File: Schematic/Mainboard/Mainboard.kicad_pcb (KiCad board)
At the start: 2 copper layers, 14 parts, among them J1 Motor_C, J2 Motor_B, J3 Motor_A, J4 Servo, J5 Servo, J6 ESC, J7 ESC_PWR, SW1 SW_DIP_x01, U1 BP, U4 XL60019_Boost_Module, U5 Mini360, U6 RFM69HW

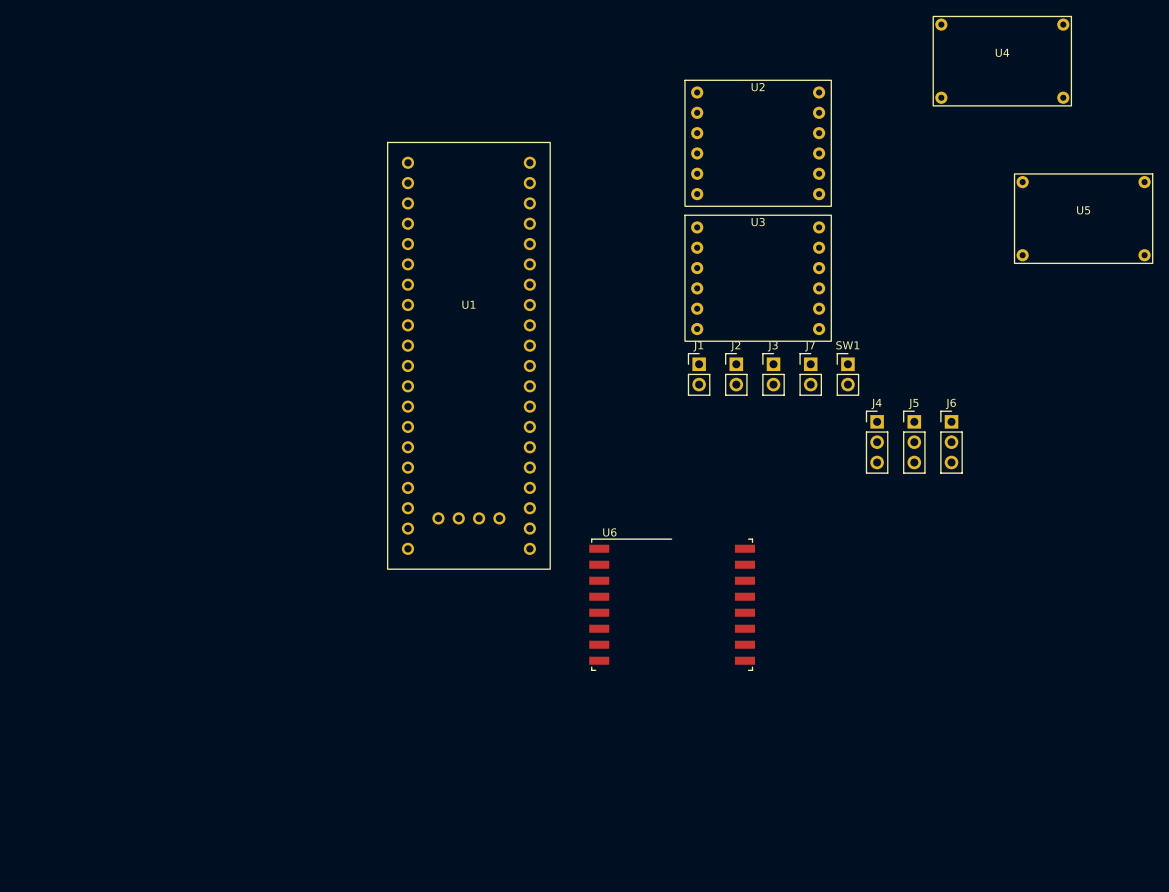
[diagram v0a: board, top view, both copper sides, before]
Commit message: PCB work
trying to cram everything on there
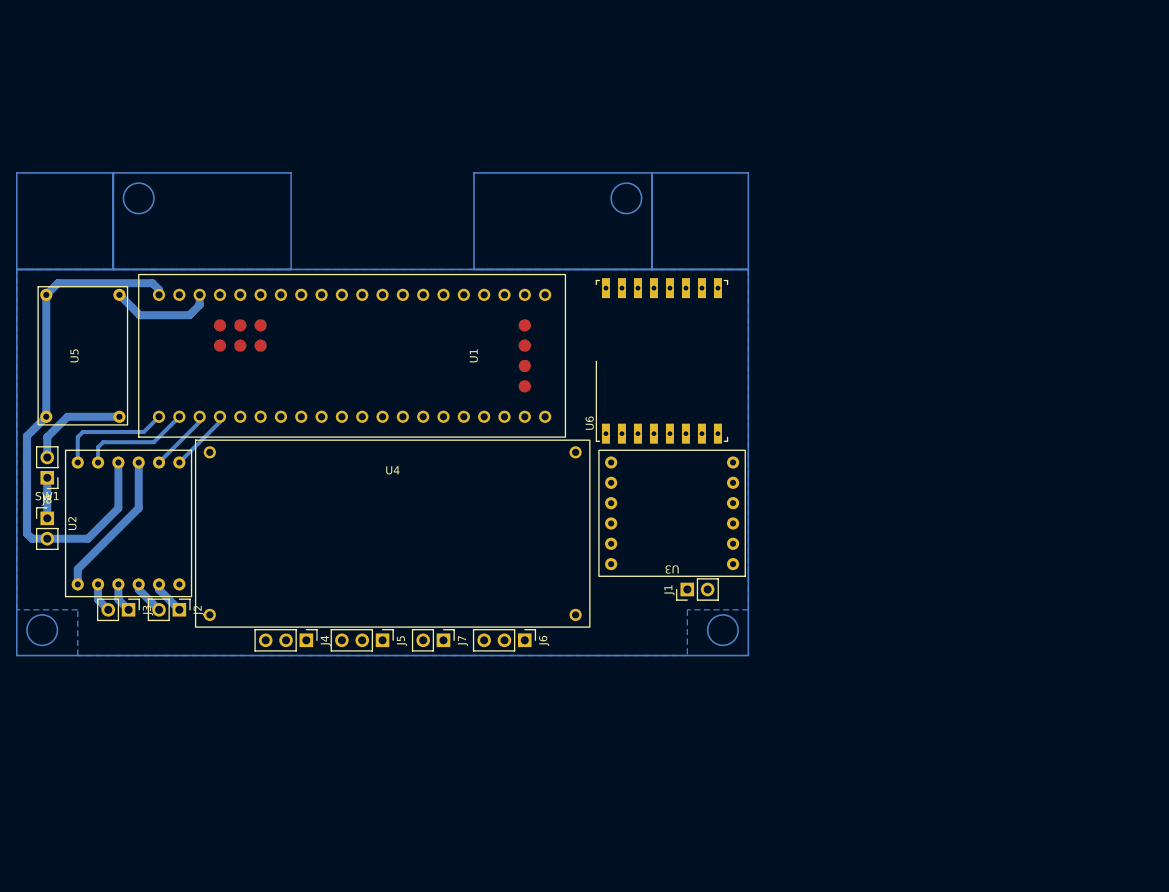
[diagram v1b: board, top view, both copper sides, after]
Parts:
- added J8: BATT_IN, Connector_PinHeader_2.54mm:PinHeader_1x02_P2.54mm_Vertical, F.Cu at (72.4, 102.9)
- SW1: value SW_DIP_x01 -> MAIN_CUTOFF
- U4: footprint My_Library:Mini360 -> My_Library:XL60019 Boost Module
- U6: footprint RF_Module:HOPERF_RFM69HW -> My_Library:HOPERF_RFM69HW
- moved U5 126.3 mm to (76.8, 82.5), turned to 90 degrees
- moved SW1 101.1 mm to (72.4, 97.8), turned to 180 degrees
- moved U4 96.2 mm to (115.6, 104.5)
- moved U2 93.7 mm to (81.3, 103.5), turned to 90 degrees
- moved J3 86.3 mm to (82.6, 114.3), turned to -90 degrees
- moved J4 76.4 mm to (104.8, 118.1), turned to -90 degrees
- moved J2 76.1 mm to (88.9, 114.3), turned to -90 degrees
- moved J5 71.9 mm to (114.3, 118.1), turned to -90 degrees
- moved J6 59.9 mm to (132.1, 118.1), turned to -90 degrees
- moved J7 57.4 mm to (121.9, 118.1), turned to -90 degrees
- moved U3 33.7 mm to (150.5, 103.5), turned to 180 degrees
- moved U6 30.5 mm to (149.2, 83.2), turned to 90 degrees
- moved J1 28.2 mm to (152.4, 111.8), turned to 90 degrees
- moved U1 15.9 mm to (109.2, 82.5), turned to 90 degrees
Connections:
- U1 pad PA0: /M B1 -> unconnected-(U1-PadPA0)
- U1 pad PA1: /M B2 -> unconnected-(U1-PadPA1)
- U1 pad PA10: unconnected-(U1-PadPA10) -> /ESC
- U1 pad PA2: /M C1 -> unconnected-(U1-PadPA2)
- U1 pad PA3: /M C2 -> unconnected-(U1-PadPA3)
- U1 pad PA8: unconnected-(U1-PadPA8) -> /SERVO 2
- U1 pad PA9: unconnected-(U1-PadPA9) -> /SERVO 1
- U1 pad PB12: unconnected-(U1-PadPB12) -> /M B2
- U1 pad PB13: unconnected-(U1-PadPB13) -> /M B1
- U1 pad PB14: unconnected-(U1-PadPB14) -> /M A2
- U1 pad PB15: unconnected-(U1-PadPB15) -> /M A1
- U1 pad PB7: /ESC -> unconnected-(U1-PadPB7)
- U1 pad PB8: /SERVO 2 -> /M C2
- U1 pad PB9: /SERVO 1 -> /M C1
- U1 pad PC14: /M A1 -> unconnected-(U1-PadPC14)
- U1 pad PC15: /M A2 -> unconnected-(U1-PadPC15)
- U1 pad SWO: (no net) -> unconnected-(U1-PadSWO)
- U2 pad 1: +3V3 -> +12V
- U3 pad 1: +3V3 -> +12V
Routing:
- net GND: track 0.00 -> 65.5 mm
- net +12V: track 0.00 -> 18.4 mm
- net /M B2: track 0.00 -> 14.4 mm
- net /M B1: track 0.00 -> 13.6 mm
- net +3V3: track 0.00 -> 12.9 mm
- net /+BATT SW: track 0.00 -> 12.6 mm
- net /M A2: track 0.00 -> 7.82 mm
- net /M A1: track 0.00 -> 7.82 mm
- net +BATT: track 0.00 -> 5.08 mm
- net Net-(J2-Pin_2): track 0.00 -> 4.23 mm
- net Net-(J2-Pin_1): track 0.00 -> 4.23 mm
- net Net-(J3-Pin_2): track 0.00 -> 3.71 mm
- net Net-(J3-Pin_1): track 0.00 -> 3.70 mm
- added copper zone on B.Cu, net GND

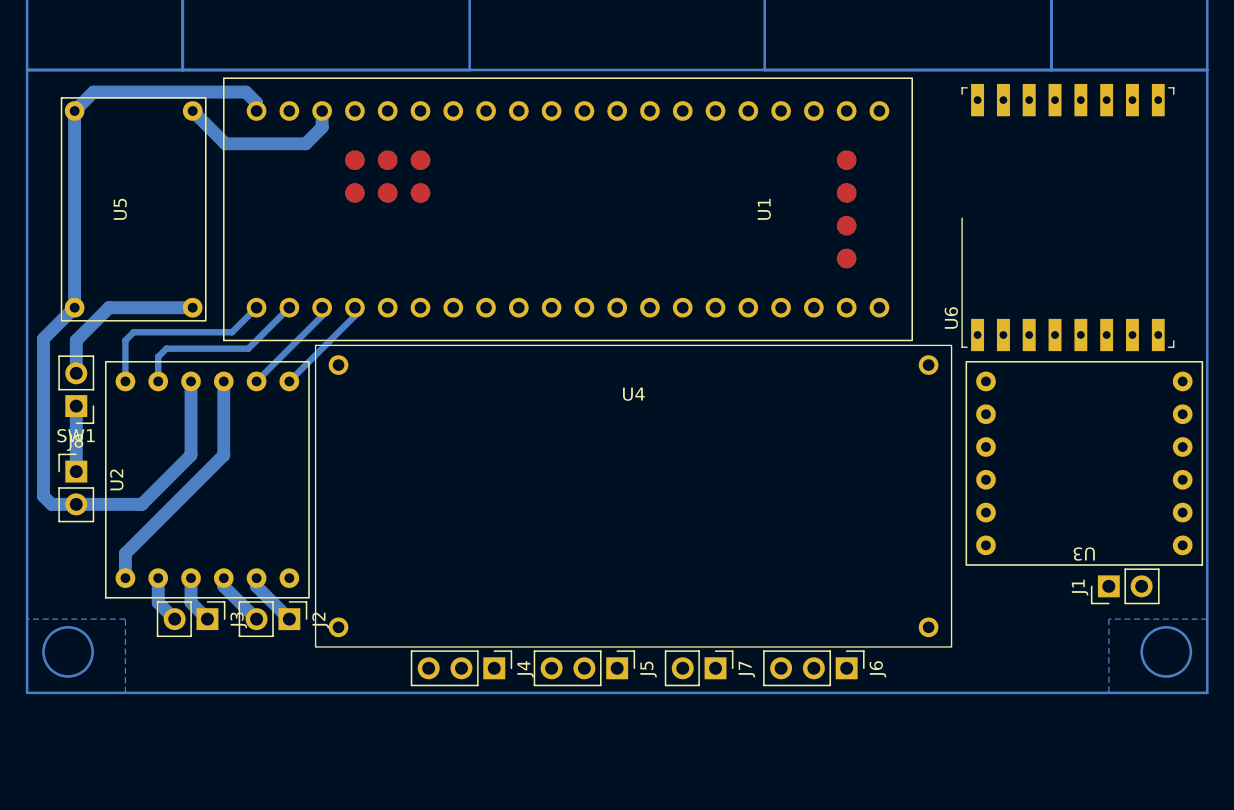
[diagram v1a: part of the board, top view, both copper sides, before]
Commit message: shift from STM32 to ESP32
on the robot control surface
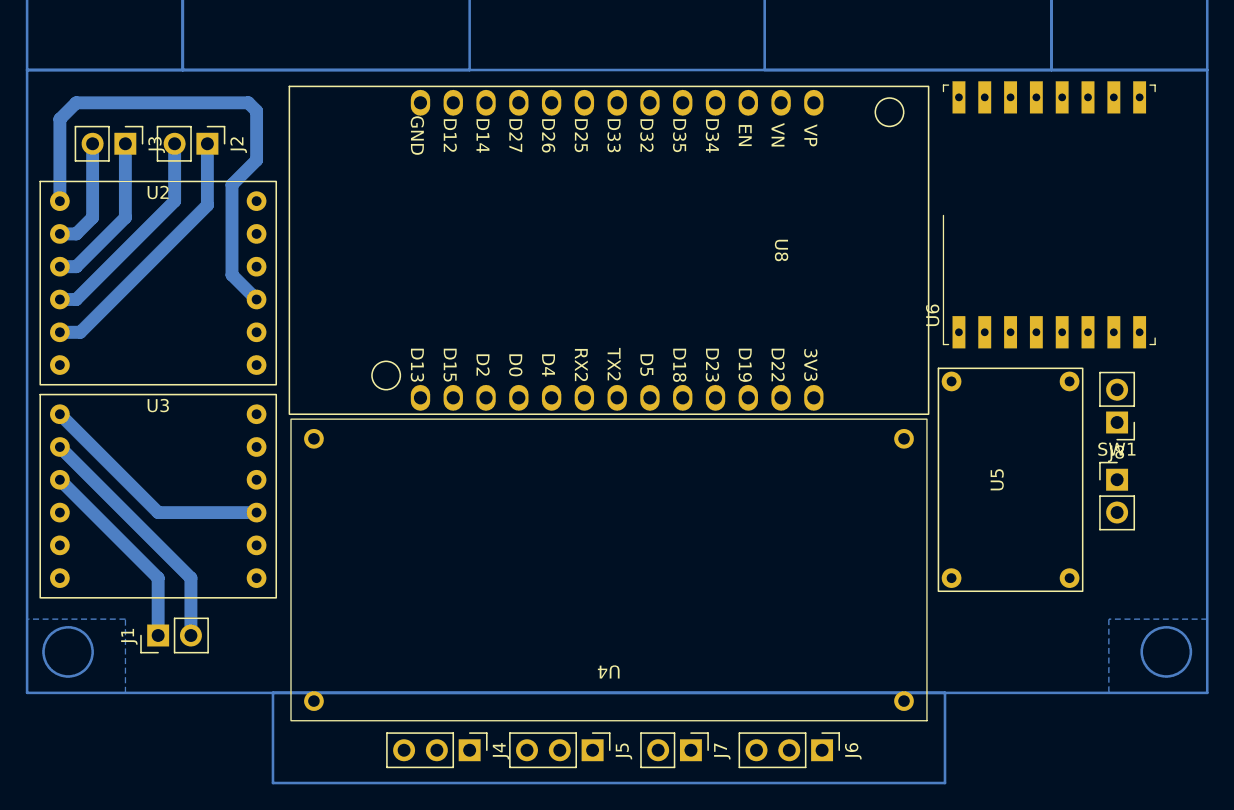
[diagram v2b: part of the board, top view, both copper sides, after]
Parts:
- removed U1: BP, My_Library:blue_pill
- added U8: ESP32-LOLIN32-Lite, Espressif:ESP32-LOLIN32-Lite, F.Cu at (114.3, 85.7)
- moved SW1 80.8 mm to (153.0, 103.5), turned to 0 degrees
- moved J8 80.7 mm to (153.0, 99.1), turned to 180 degrees
- moved J1 73.8 mm to (78.7, 115.6)
- moved U3 71.8 mm to (78.7, 103.5), turned to 0 degrees
- moved U5 71.1 mm to (144.8, 103.5)
- moved J3 37.4 mm to (76.2, 77.5)
- moved J2 37.4 mm to (82.5, 77.5)
- moved U2 16.7 mm to (78.7, 87.0), turned to 0 degrees
- moved J4 6.63 mm to (102.9, 124.5)
- moved J5 6.63 mm to (112.4, 124.5)
- moved J6 6.63 mm to (130.2, 124.5)
- moved J7 6.63 mm to (120.0, 124.5)
- moved U4 6.51 mm to (113.7, 110.7), turned to 180 degrees
- moved U6 1.46 mm to (147.8, 83.0)
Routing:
- net GND: track 65.5 -> 0.00 mm
- net +12V: track 18.4 -> 57.0 mm
- net Net-(J1-Pin_2): track 0.00 -> 18.8 mm
- net Net-(J2-Pin_1): track 4.23 -> 20.3 mm
- net Net-(J1-Pin_1): track 0.00 -> 15.2 mm
- net /M B2: track 14.4 -> 0.00 mm
- net /M B1: track 13.6 -> 0.00 mm
- net +3V3: track 12.9 -> 0.00 mm
- net /+BATT SW: track 12.6 -> 0.00 mm
- net Net-(J2-Pin_2): track 4.23 -> 16.5 mm
- net Net-(J3-Pin_1): track 3.70 -> 12.4 mm
- net /M A2: track 7.82 -> 0.00 mm
- net /M A1: track 7.82 -> 0.00 mm
- net +BATT: track 5.08 -> 0.00 mm
- net Net-(J3-Pin_2): track 3.71 -> 8.78 mm

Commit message: update schematic and CAD
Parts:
- moved U4 1.65 mm to (114.3, 109.2)
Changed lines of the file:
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@@
   )
   (footprint "My_Library:XL60019 Boost Module" (layer "F.Cu")
-    (at 113.665 110.744 180)
+    (at 114.3 109.22 180)
     (property "Sheetfile" "Mainboard.kicad_sch")
     (property "Sheetname" "")
@@
         (effects (font (size 1 1) (thickness 0.15)))
     )
-    (fp_rect (start -24.638 -11.43) (end 24.638 11.938)
+    (fp_rect (start -21.59 -10.16) (end 21.59 10.16)
       (stroke (width 0.1) (type default)) (fill none) (layer "F.SilkS"))
-    (fp_rect (start -22.86 -9.906) (end 22.86 10.414)
+    (fp_rect (start -20.32 -8.89) (end 20.32 8.89)
       (stroke (width 0.1) (type default)) (fill none) (layer "User.1"))
-    (fp_rect (start -12.7 -7.366) (end -2.54 2.794)
+    (fp_rect (start -10.16 -3.81) (end 0 6.35)
       (stroke (width 0.1) (type default)) (fill none) (layer "User.1"))
-    (fp_rect (start 0 -4.826) (end 10.16 5.334)
+    (fp_rect (start -1.27 -8.89) (end -10.16 -5.08)
       (stroke (width 0.1) (type default)) (fill none) (layer "User.1"))
-    (fp_circle (center -18.832102 0.254) (end -21.372102 -2.286)
+    (fp_circle (center -15.24 0) (end -19.05 0)
       (stroke (width 0.1) (type default)) (fill none) (layer "User.1"))
-    (fp_circle (center 17.78 2.794) (end 15.24 0.254)
+    (fp_circle (center 15.24 0) (end 19.05 0)
       (stroke (width 0.1) (type default)) (fill none) (layer "User.1"))
     (fp_poly
       (pts
-        (xy 2.54 -2.286)
-        (xy 2.54 2.794)
-        (xy 7.62 0.254)
+        (xy -7.62 -1.27)
+        (xy -7.62 3.81)
+        (xy -2.54 1.27)
       )
       (stroke (width 0.1) (type solid)) (fill none) (layer "User.1"))
-    (pad "1" thru_hole circle (at -22.86 10.414 180) (size 1.524 1.524) (drill 0.9) (layers "*.Cu" "*.Mask")
+    (pad "1" thru_hole circle (at -20.32 8.89 180) (size 1.524 1.524) (drill 0.762) (layers "*.Cu" "*.Mask")
       (net 9 "GND") (pinfunction "GND") (pintype "power_in"))
-    (pad "2" thru_hole circle (at -22.86 -9.906 180) (size 1.524 1.524) (drill 0.9) (layers "*.Cu" "*.Mask")
+    (pad "2" thru_hole circle (at -20.32 -8.89 180) (size 1.524 1.524) (drill 0.762) (layers "*.Cu" "*.Mask")
       (net 8 "/+BATT SW") (pinfunction "IN") (pintype "power_in"))
-    (pad "3" thru_hole circle (at 22.86 10.414 180) (size 1.524 1.524) (drill 0.9) (layers "*.Cu" "*.Mask")
+    (pad "3" thru_hole circle (at 20.32 8.89 180) (size 1.524 1.524) (drill 0.762) (layers "*.Cu" "*.Mask")
       (net 9 "GND") (pinfunction "GND") (pintype "power_out"))
-    (pad "4" thru_hole circle (at 22.86 -9.906 180) (size 1.524 1.524) (drill 0.9) (layers "*.Cu" "*.Mask")
+    (pad "4" thru_hole circle (at 20.32 -8.89 180) (size 1.524 1.524) (drill 0.762) (layers "*.Cu" "*.Mask")
       (net 30 "+12V") (pinfunction "OUT") (pintype "power_out"))
   )

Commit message: finish first revision PCB
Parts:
- added D1: 1N4007, Diode_THT:D_DO-41_SOD81_P7.62mm_Horizontal, F.Cu at (133.3, 123.2)
- added F1: Fuse 15A, Connector_PinHeader_2.54mm:PinHeader_1x02_P2.54mm_Vertical, F.Cu at (158.1, 144.8)
- added F2: Fuse 15A, Connector_PinHeader_2.54mm:PinHeader_1x02_P2.54mm_Vertical, F.Cu at (181.6, 120.0)
- moved J1 119.9 mm to (195.6, 88.9), turned to 0 degrees
- moved J2 113.1 mm to (195.6, 82.5), turned to 0 degrees
- moved J3 113.1 mm to (191.8, 120.0), turned to -90 degrees
- moved U2 108.1 mm to (186.7, 108.6), turned to 90 degrees
- moved U3 105.4 mm to (184.2, 88.3), turned to 180 degrees
- moved J5 79.7 mm to (181.6, 136.5), turned to 0 degrees
- moved J6 74.0 mm to (185.4, 136.5), turned to 0 degrees
- moved J7 60.3 mm to (189.2, 136.5), turned to 0 degrees
- moved J8 52.4 mm to (168.3, 144.8), turned to 90 degrees
- moved U6 50.3 mm to (188.6, 128.3), turned to 0 degrees
- moved U5 48.9 mm to (157.5, 132.1), turned to 0 degrees
- moved J4 47.1 mm to (141.6, 144.8), turned to -90 degrees
- moved U1 46.6 mm to (154.9, 108.6)
- moved SW1 41.6 mm to (147.9, 144.8), turned to 90 degrees
- moved U4 8.76 mm to (139.7, 86.4), turned to 0 degrees
- renumbered J3 to J1, J1 to J3, J8 to J4, J4 to J5, J5 to J6, J6 to J7, J7 to J8, U8 to U1, U3 to U2, U2 to U3, U6 to U4, U4 to U5, U5 to U6
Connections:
- J3 pad 1: Net-(J1-Pin_1) (its old number) -> Net-(J3-Pin_1)
- J3 pad 2: Net-(J1-Pin_2) (its old number) -> Net-(J3-Pin_2)
- SW1 pad 2: /+BATT SW -> Net-(F1-Pad1)
- U1 pad 12: /MISO -> /NSS
- U1 pad 14: /NSS -> /MISO
- U1 pad 22: /SLEEP -> unconnected-(U1-D2-Pad22)
- U1 pad 23: /SERVO 2 -> /SERVO 1
- U1 pad 24: /SERVO 1 -> /SERVO 2
- U1 pad 27: /M C2 -> /M A1
- U1 pad 34: /M C1 -> /M A2
- U1 pad 38: /M A2 -> /M C2
- U1 pad 39: /M A1 -> /M C1
- U2 pad 11: unconnected-(U3-IN3-Pad11) -> /M C1
- U2 pad 12: unconnected-(U3-IN4-Pad12) -> /M C2
- U2 pad 2: Net-(J1-Pin_2) (its old number) -> unconnected-(U2-OUT1-Pad2)
- U2 pad 3: Net-(J1-Pin_1) (its old number) -> unconnected-(U2-OUT2-Pad3)
- U2 pad 4: unconnected-(U3-OUT3-Pad4) -> Net-(J3-Pin_2)
- U2 pad 5: unconnected-(U3-OUT4-Pad5) -> Net-(J3-Pin_1)
- U2 pad 7: /M C1 -> unconnected-(U2-IN1-Pad7)
- U2 pad 8: /M C2 -> unconnected-(U2-IN2-Pad8)
- U5 pad 2: /+BATT SW -> Net-(D1-K)
- U5 pad 4: +12V -> Net-(U5-OUT)
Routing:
- net +3V3: track 0.00 -> 92.3 mm
- net GND: track 0.00 -> 81.3 mm
- net /+BATT SW: track 0.00 -> 69.9 mm
- net /M A1: track 0.00 -> 49.4 mm
- net /SERVO 1: track 0.00 -> 47.4 mm
- net /ESC: track 0.00 -> 47.2 mm
- net /SERVO 2: track 0.00 -> 46.9 mm
- net /M A2: track 0.00 -> 45.8 mm
- net /M B1: track 0.00 -> 36.6 mm
- net /M B2: track 0.00 -> 33.5 mm
- net /M C1: track 0.00 -> 29.6 mm
- net /M C2: track 0.00 -> 28.9 mm
- net /RESET: track 0.00 -> 25.6 mm
- net /INTER: track 0.00 -> 22.4 mm
- net /NSS: track 0.00 -> 21.5 mm
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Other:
- board outline added: 70 x 70 mm
